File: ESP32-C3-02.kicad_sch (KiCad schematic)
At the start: 31 parts, among them J3 GSD090012SEU, U3 ESP32-C3-WROOM-02-H4, U4 CP2102N-Axx-xQFN20, U5 USBLC6-2SC6, U6 W25Q32JVSSIQ

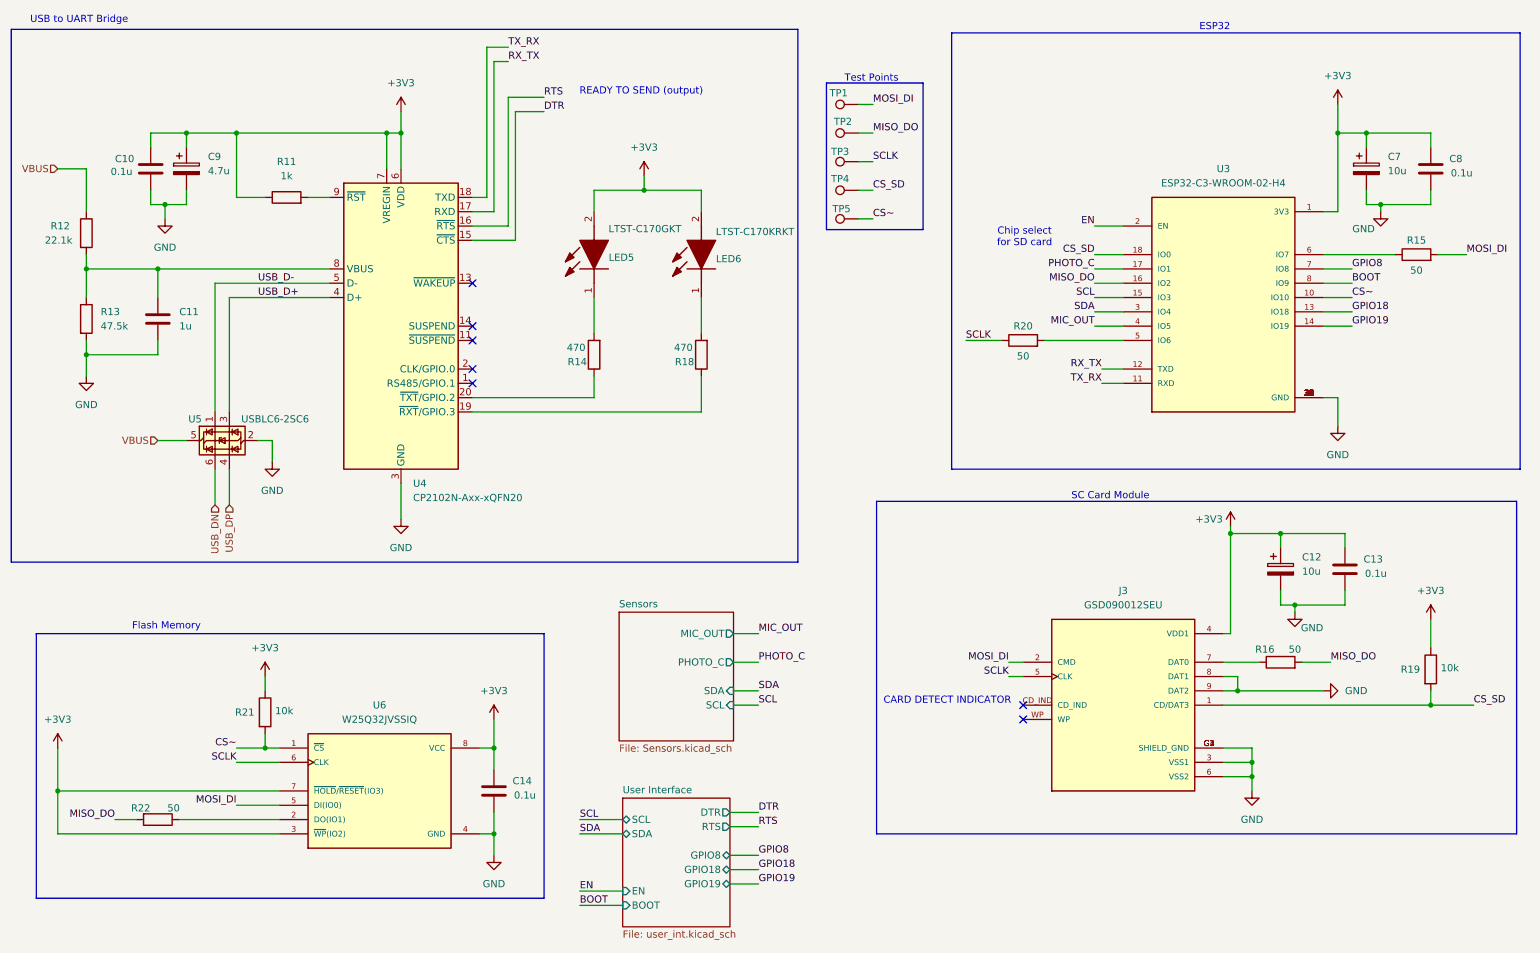
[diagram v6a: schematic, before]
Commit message: finalized edge cuts and component placement
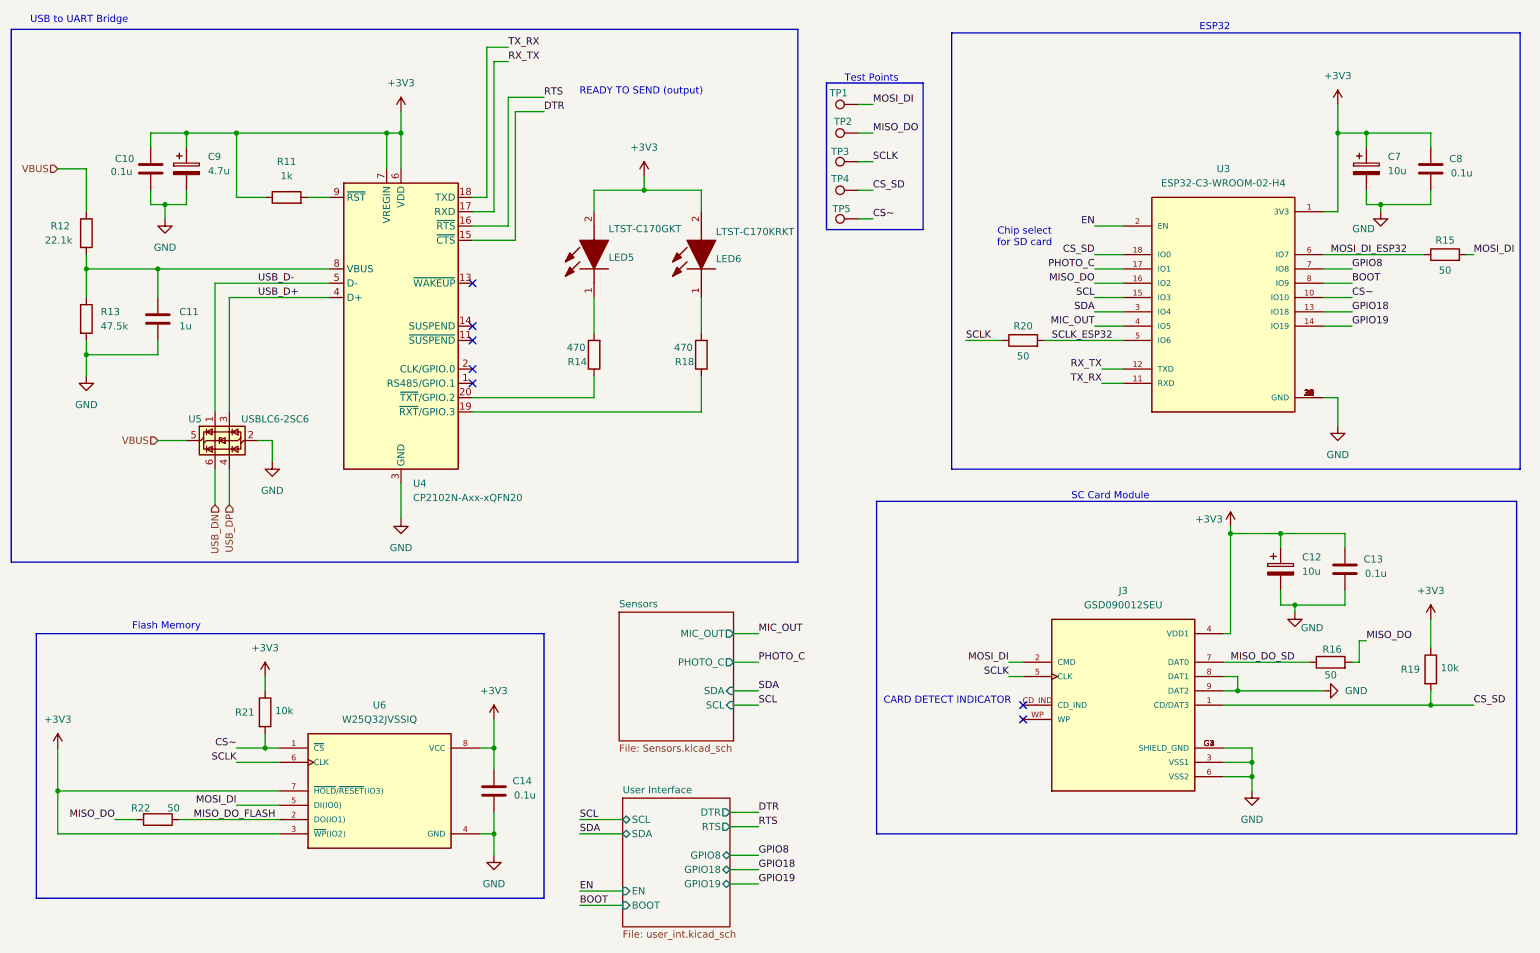
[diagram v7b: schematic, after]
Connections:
- net SCLK_ESP32: now reaches R20.2, U3.5 (IO6)
- net MISO_DO_FLASH: now reaches R22.1, U6.2 (DO(IO1))
- net MOSI_DI_ESP32: now reaches R15.1, U3.6 (IO7)
- net MISO_DO_SD: now reaches J3.7 (DAT0), R16.1
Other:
- moved on the sheet: R15, R16
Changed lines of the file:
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@@
 	(wire
 		(pts
-			(xy 243.84 133.35) (xy 248.92 133.35)
+			(xy 254 129.54) (xy 255.27 129.54)
 		)
 		(stroke
@@
 	(wire
 		(pts
+			(xy 254 133.35) (xy 252.73 133.35)
+		)
+		(stroke
+			(width 0)
+			(type default)
+		)
+	)
+	(wire
+		(pts
 			(xy 60.96 93.98) (xy 58.42 93.98)
 		)
@@
 	(wire
 		(pts
-			(xy 229.87 133.35) (xy 236.22 133.35)
+			(xy 229.87 133.35) (xy 245.11 133.35)
 		)
 		(stroke
@@
 	(wire
 		(pts
-			(xy 267.97 60.96) (xy 273.05 60.96)
+			(xy 273.05 60.96) (xy 274.32 60.96)
 		)
 		(stroke
@@
 	(wire
 		(pts
-			(xy 247.65 60.96) (xy 260.35 60.96)
+			(xy 247.65 60.96) (xy 265.43 60.96)
 		)
 		(stroke
@@
 	(wire
 		(pts
+			(xy 254 129.54) (xy 254 133.35)
+		)
+		(stroke
+			(width 0)
+			(type default)
+		)
+	)
+	(wire
+		(pts
 			(xy 127 49.53) (xy 137.16 49.53)
 		)
@@
 	)
 	(label "MOSI_DI"
-		(at 273.05 60.96 0)
+		(at 274.32 60.96 0)
 		(effects
 			(font
@@
 		)
 	)
+	(label "SCLK_ESP32"
+		(at 199.39 76.2 0)
+		(effects
+			(font
+				(size 1.27 1.27)
+			)
+			(justify left bottom)
+		)
+	)
 	(label "TX_RX"
 		(at 102.87 24.13 0)
@@
 		)
 	)
+	(label "MISO_DO_FLASH"
+		(at 46.99 161.29 0)
+		(effects
+			(font
+				(size 1.27 1.27)
+			)
+			(justify left bottom)
+		)
+	)
 	(label "GPIO8"
 		(at 252.73 63.5 0)
@@
 	)
 	(label "MISO_DO"
-		(at 248.92 133.35 0)
+		(at 255.27 129.54 0)
 		(effects
 			(font
@@
 		)
 	)
+	(label "MOSI_DI_ESP32"
+		(at 248.92 60.96 0)
+		(effects
+			(font
+				(size 1.27 1.27)
+			)
+			(justify left bottom)
+		)
+	)
 	(label "SCL"
 		(at 207.01 68.58 180)
@@
 		)
 	)
+	(label "MISO_DO_SD"
+		(at 231.14 133.35 0)
+		(effects
+			(font
+				(size 1.27 1.27)
+			)
+			(justify left bottom)
+		)
+	)
 	(label "SCL"
 		(at 115.57 161.29 0)
@@
 	(symbol
 		(lib_id "Device:R")
-		(at 264.16 60.96 90)
+		(at 269.24 60.96 90)
 		(unit 1)
 		(body_style 1)
@@
 		(dnp no)
 		(property "Reference" "R15"
-			(at 264.16 58.42 90)
+			(at 269.24 58.42 90)
 			(show_name no)
 			(do_not_autoplace no)
@@
 		)
 		(property "Value" "50"
-			(at 264.16 63.754 90)
+			(at 269.24 63.754 90)
 			(show_name no)
 			(do_not_autoplace no)
@@
 		)
 		(property "Footprint" "Resistor_SMD:R_0805_2012Metric"
-			(at 264.16 62.738 90)
+			(at 269.24 62.738 90)
 			(hide yes)
 			(show_name no)
@@
 		)
 		(property "Datasheet" ""
-			(at 264.16 60.96 0)
+			(at 269.24 60.96 0)
 			(hide yes)
 			(show_name no)
@@
 		)
 		(property "Description" "Resistor"
-			(at 264.16 60.96 0)
+			(at 269.24 60.96 0)
 			(hide yes)
 			(show_name no)
@@
 		)
 		(property "Purpose" ""
-			(at 264.16 60.96 0)
+			(at 269.24 60.96 0)
 			(show_name no)
 			(do_not_autoplace no)
@@
 	(symbol
 		(lib_id "Device:R")
-		(at 240.03 133.35 90)
+		(at 248.92 133.35 90)
 		(unit 1)
 		(body_style 1)
@@
 		(dnp no)
 		(property "Reference" "R16"
-			(at 237.236 131.064 90)
+			(at 249.174 131.064 90)
 			(show_name no)
 			(do_not_autoplace no)
@@
 		)
 		(property "Value" "50"
-			(at 242.57 131.064 90)
+			(at 248.92 135.636 90)
 			(show_name no)
 			(do_not_autoplace no)
@@
 		)
 		(property "Footprint" "Resistor_SMD:R_0805_2012Metric"
-			(at 240.03 135.128 90)
+			(at 248.92 135.128 90)
 			(hide yes)
 			(show_name no)
@@
 		)
 		(property "Datasheet" ""
-			(at 240.03 133.35 0)
+			(at 248.92 133.35 0)
 			(hide yes)
 			(show_name no)
@@
 		)
 		(property "Description" "Resistor"
-			(at 240.03 133.35 0)
+			(at 248.92 133.35 0)
 			(hide yes)
 			(show_name no)
@@
 		)
 		(property "Purpose" ""
-			(at 240.03 133.35 0)
+			(at 248.92 133.35 0)
 			(show_name no)
 			(do_not_autoplace no)

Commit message: corrected boot control schematic and layout
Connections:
- net CS_SD: now also U3.4 (IO5); no longer U3.18 (IO0)
- net MIC_OUT: now also U3.18 (IO0); no longer U3.4 (IO5)
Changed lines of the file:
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@@
 	(text "Chip select \nfor SD card"
 		(exclude_from_sim no)
-		(at 194.564 57.912 0)
+		(at 191.77 56.642 0)
 		(effects
 			(font
@@
 		)
 	)
-	(label "CS_SD"
+	(label "MIC_OUT"
 		(at 207.01 60.96 180)
 		(effects
@@
 		)
 	)
-	(label "MIC_OUT"
+	(label "CS_SD"
 		(at 207.01 73.66 180)
 		(effects
